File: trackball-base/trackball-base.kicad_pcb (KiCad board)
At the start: 2 copper layers, 110 x 140 mm, 155 parts, among them J201 TYPE-C-31-M-12, J202 CORTEX-DBG-10, Q101 2N7002, SW201 RESET, SW202 BOOT, SW401 D2FC-F-7N, SW402 D2FC-F-7N, SW403 D2FC-F-7N, U101 AP2112K-3.3TRG1, U102 APX809-29SAG-7, U103 XC6206P192MR, U104 TPS22918DBVR, U105 TPS22918DBVR, U106 TLV3011AIDBVR, U107 TLV3011AIDBVR, U201 E73-2G4M08S1C, U202 TPD2E1B06DRLR, U301 PMW3360DM-T2QU, U302 PMW3360DM-T2QU, U501 LTC4125EUFD, Y201 ABS07-32.768KHZ-9-T

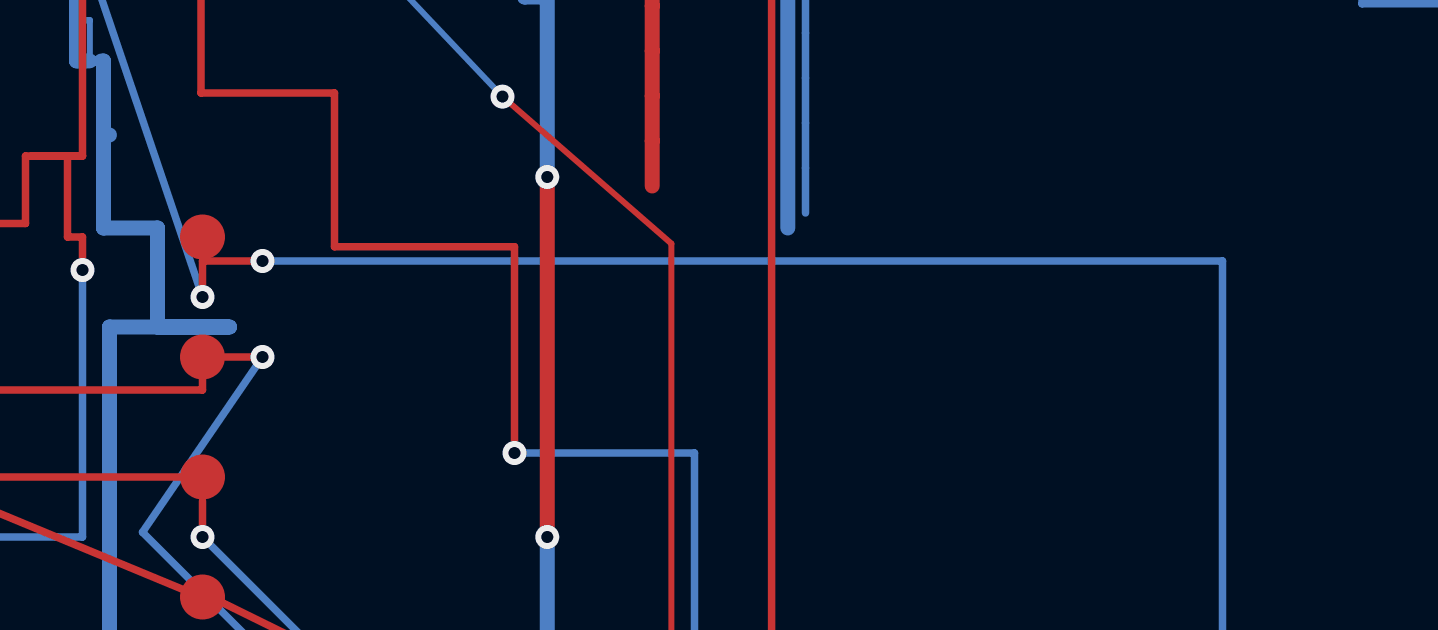
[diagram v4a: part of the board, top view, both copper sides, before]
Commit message: layout: ECO4 TP305/306 micro-move + P131 U2 east loop — drc127 26unc/0err/0parity
TP305->(44.0,43.5), TP306->(44.0,47.2), stubs kept (same-net overlap).
U2 closed via B-y=45.0/F-hop/B-x=78.8/B-y=42.0 loop around S2_SCK corner.
Q6-TP portion resolved; Q5 + Q6-remainder still await owner.
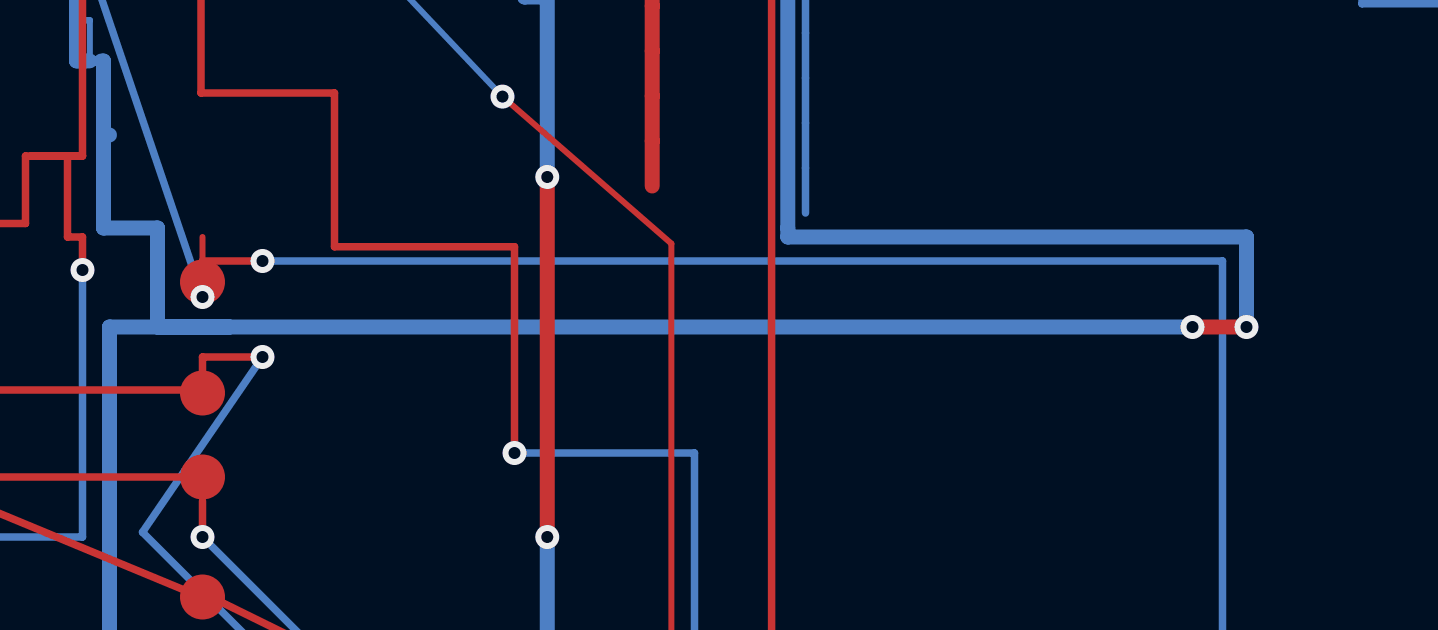
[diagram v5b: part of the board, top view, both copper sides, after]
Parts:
- moved TP305 1.50 mm to (44.0, 43.5)
- moved TP306 1.20 mm to (44.0, 47.2)
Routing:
- net +3V3: track 405.7 -> 458.2 mm, vias 22 -> 24
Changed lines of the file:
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@@
 	(footprint "TestPoint:TestPoint_Pad_D1.5mm"
 		(layer "F.Cu")
-		(at 44 42)
+		(at 44 43.5)
 		(descr "SMD pad as test Point, diameter 1.5mm")
 		(tags "test point SMD pad")
@@
 	(footprint "TestPoint:TestPoint_Pad_D1.5mm"
 		(layer "F.Cu")
-		(at 44 46)
+		(at 44 47.2)
 		(descr "SMD pad as test Point, diameter 1.5mm")
 		(tags "test point SMD pad")
@@
 	)
 	(segment
+		(start 77 45)
+		(end 78.8 45)
+		(width 0.5)
+		(layer "F.Cu")
+		(net "+3V3")
+	)
+	(segment
 		(start 25 20.6)
 		(end 25 20.09)
@@
 	)
 	(via
+		(at 77 45)
+		(size 0.8)
+		(drill 0.4)
+		(layers "F.Cu" "B.Cu")
+		(net "+3V3")
+	)
+	(via
 		(at 35 26.6)
 		(size 0.8)
@@
 	)
 	(via
+		(at 78.8 45)
+		(size 0.8)
+		(drill 0.4)
+		(layers "F.Cu" "B.Cu")
+		(net "+3V3")
+	)
+	(via
 		(at 14.1542 22.9815)
 		(size 0.6)
@@
 	)
 	(segment
+		(start 78.8 42)
+		(end 63.51 42)
+		(width 0.5)
+		(layer "B.Cu")
+		(net "+3V3")
+	)
+	(segment
 		(start 14.1542 22.9815)
 		(end 12.6152 21.4425)
@@
 	)
 	(segment
+		(start 78.8 45)
+		(end 78.8 42)
+		(width 0.5)
+		(layer "B.Cu")
+		(net "+3V3")
+	)
+	(segment
 		(start 75.725 81.34)
 		(end 75.725 85.97)
@@
 	)
 	(segment
+		(start 63.51 42)
+		(end 63.51 41.7)
+		(width 0.5)
+		(layer "B.Cu")
+		(net "+3V3")
+	)
+	(segment
 		(start 39.825 34.775)
 		(end 40.245 34.775)
@@
 		(width 0.5)
 		(layer "B.Cu")
+		(net "+3V3")
+	)
+	(segment
+		(start 44.9 45)
+		(end 77 45)
+		(width 0.5)
+		(layer "B.Cu")

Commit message: Q5 ECO + pre-ripup checkpoint: R113/114/115/515 jumpers, drc129 33unc/0err/0parity
Schematic (owner-approved 2026-10-04): 3x 0R branch jumpers on power
sheet (R113 VBUS_SENSE, R114 SENSOR_EN, R115 MCU_TX_EN) + R515 CTD
in-line on tx (net split /tx/CTD_U501 + /tx/Net-(U501-CTD)). ERC 0
errors + 1 known benign warning; netlist diff minimal (4 nets only).
PCB: 4x 0603 staged, nets assigned, U501.14 on CTD_U501; 0 parity.
Docs: SCHEMATIC_REVIEW §11, BOM row, LAYOUT_REVIEW E53, QUESTIONS.
Reversible checkpoint before Q6 ripup.
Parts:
- added R113: 0R, Resistor_SMD:R_0603_1608Metric, F.Cu at (92.0, 120.0)
- added R114: 0R, Resistor_SMD:R_0603_1608Metric, F.Cu at (92.0, 110.0)
- added R115: 0R, Resistor_SMD:R_0603_1608Metric, F.Cu at (92.0, 100.0)
- added R515: 0R, Resistor_SMD:R_0603_1608Metric, F.Cu at (92.0, 90.0)
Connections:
- U501 pad 14: /tx/Net-(U501-CTD) -> /tx/CTD_U501

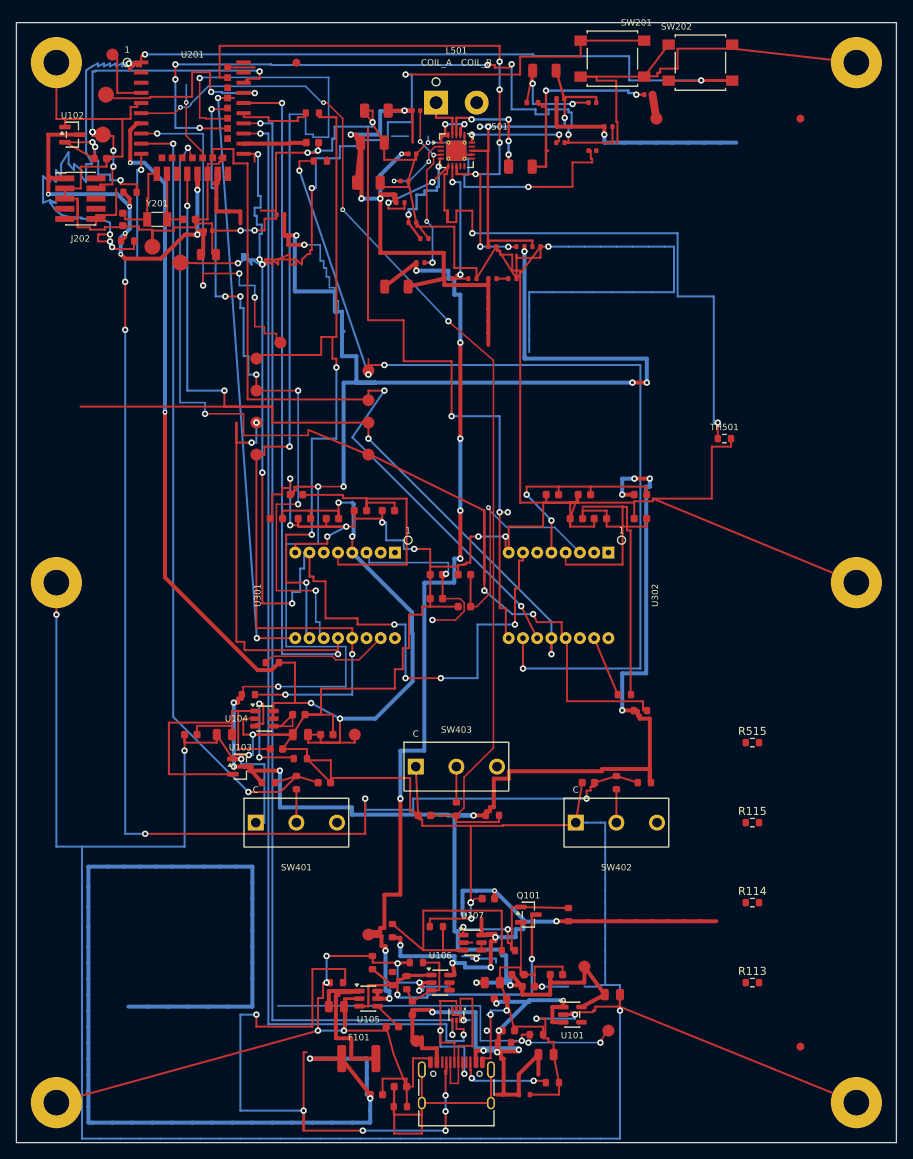
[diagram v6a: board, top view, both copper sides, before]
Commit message: Q6: 5 B-jogs for SENSOR_EN corridor (TX_EN/Pin4/S1_NCS/BTN3/P1.11) + restore SENSOR_EN B-run; drc131c 32unc/0err/0parity
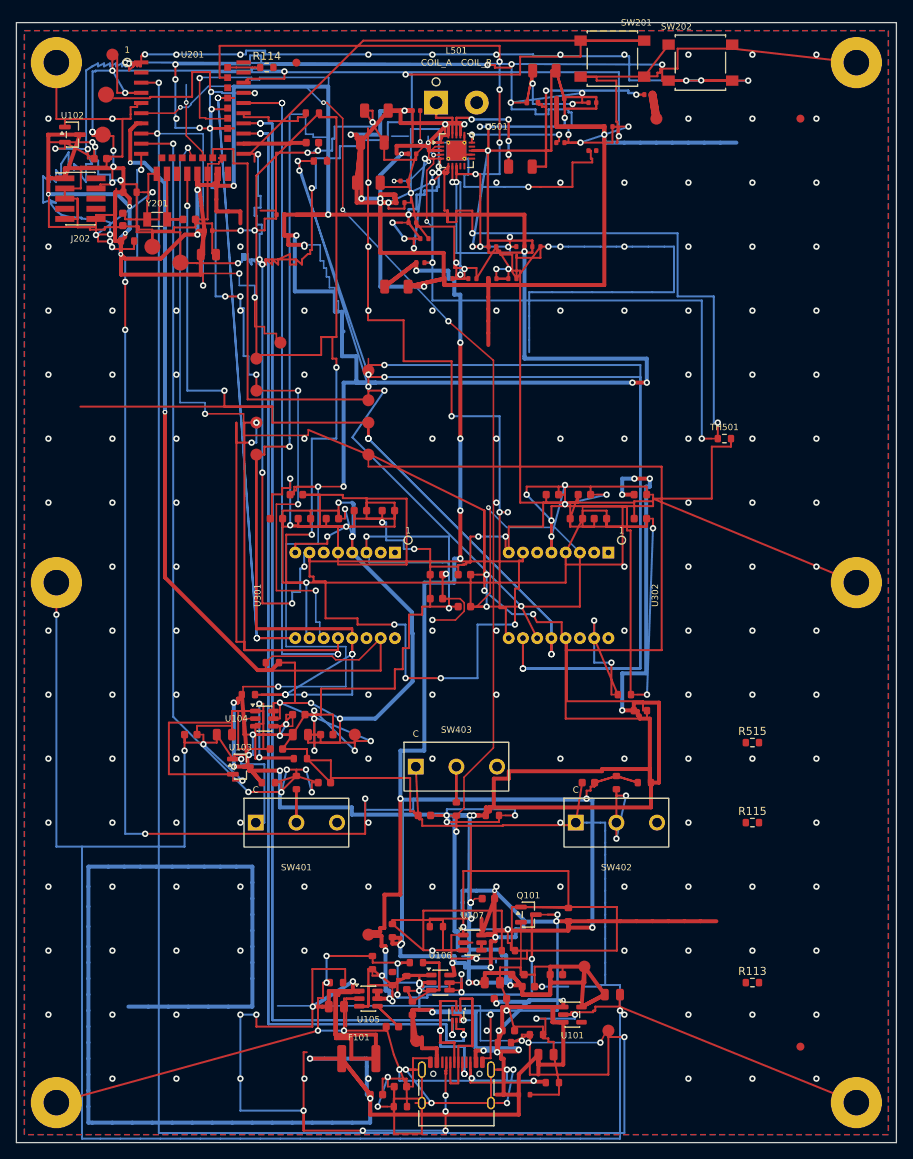
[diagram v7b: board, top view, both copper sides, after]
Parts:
- moved R114 120.8 mm to (31.3, 5.61)
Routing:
- net +3V3: track 458.2 -> 702.8 mm, vias 24 -> 28
- net VBUS_SENSE: track 49.3 -> 280.3 mm, vias 3 -> 5
- net /mcu/Net-(U201-D-): track 144.4 -> 288.9 mm, vias 2 -> 4
- net VSEN_1V9: track 222.8 -> 365.9 mm, vias 6 -> 16
- net /mcu/Net-(U201-D+): track 141.8 -> 283.6 mm, vias 2 -> 4
- net VBUS: track 298.9 -> 440.6 mm, vias 15 -> 17
- net MCU_RST: track 270.0 -> 409.5 mm, vias 15 -> 19
- net VIN: track 122.2 -> 254.9 mm, vias 8 -> 10
- net S1_MISO: track 131.3 -> 257.2 mm, vias 4 -> 6
- net S2_SCK: track 122.2 -> 245.4 mm, vias 4 -> 8
- net S2_NCS: track 130.7 -> 226.5 mm
- net /tx/Net-(U501-NTC): track 89.8 -> 182.4 mm, vias 4 -> 8
- net /mcu/Net-(U201-P1.11): track 156.8 -> 243.2 mm, vias 6 -> 10
- net TX_EN: track 83.9 -> 168.5 mm, vias 6 -> 10
- net S1_MOT: track 75.3 -> 150.6 mm, vias 2 -> 4
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- added copper zone on B.Cu, net GND
- added copper zone on F.Cu, net GND

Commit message: Q6: clean redo of 5 B-jogs + R114 place + SENSOR_EN B-run restore; drc132b 32unc/0err/0parity (reverts route.py autoroute pollution in 5f0bad7)
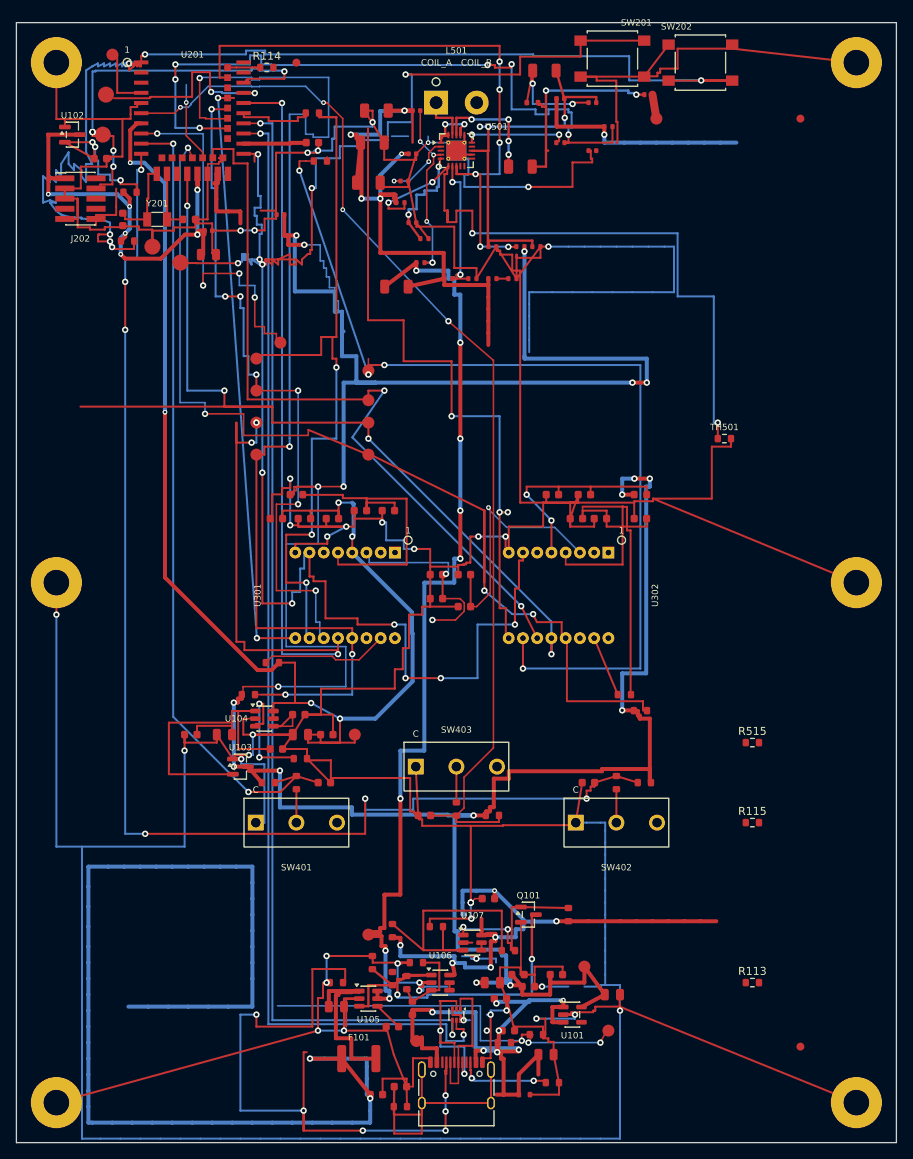
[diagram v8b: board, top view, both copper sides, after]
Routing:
- net +3V3: track 702.8 -> 458.2 mm, vias 28 -> 24
- net VBUS_SENSE: track 280.3 -> 49.3 mm, vias 5 -> 3
- net /mcu/Net-(U201-D-): track 288.9 -> 144.4 mm, vias 4 -> 2
- net VSEN_1V9: track 365.9 -> 222.8 mm, vias 16 -> 6
- net /mcu/Net-(U201-D+): track 283.6 -> 141.8 mm, vias 4 -> 2
- net VBUS: track 440.6 -> 298.9 mm, vias 17 -> 15
- net MCU_RST: track 409.5 -> 270.0 mm, vias 19 -> 15
- net VIN: track 254.9 -> 122.2 mm, vias 10 -> 8
- net S1_MISO: track 257.2 -> 131.3 mm, vias 6 -> 4
- net S2_SCK: track 245.4 -> 122.2 mm, vias 8 -> 4
- net S2_NCS: track 226.5 -> 130.7 mm
- net /tx/Net-(U501-NTC): track 182.4 -> 89.8 mm, vias 8 -> 4
- net /mcu/Net-(U201-P1.11): track 243.2 -> 157.8 mm, vias 10 -> 6
- net TX_EN: track 168.5 -> 86.2 mm, vias 10 -> 6
- net S1_MOT: track 150.6 -> 75.3 mm, vias 4 -> 2
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- removed copper zone on B.Cu, net GND
- removed copper zone on F.Cu, net GND
